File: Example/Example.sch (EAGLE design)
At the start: 9 parts, among them IC1 LM555D, J1 UX60-MB-5S8, SW1 MFS101D-6-Z

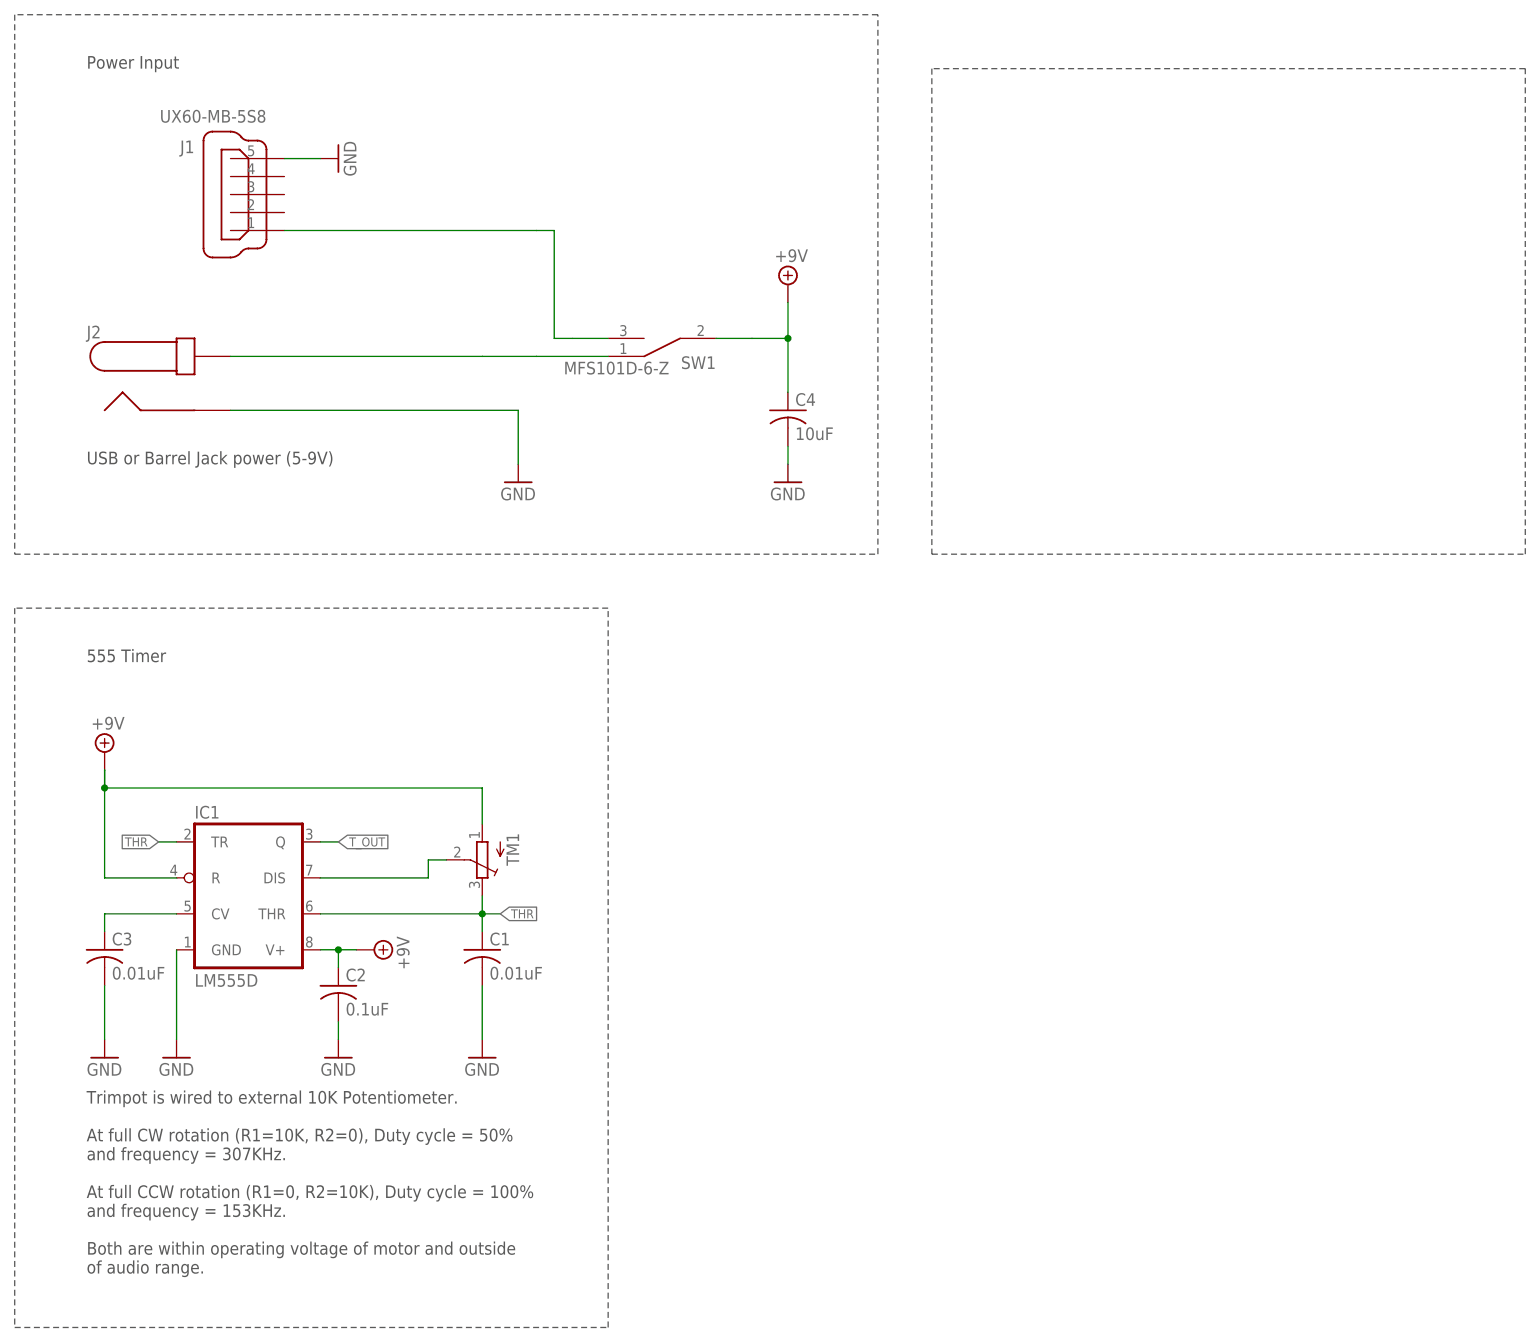
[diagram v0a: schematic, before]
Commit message: add
add parts
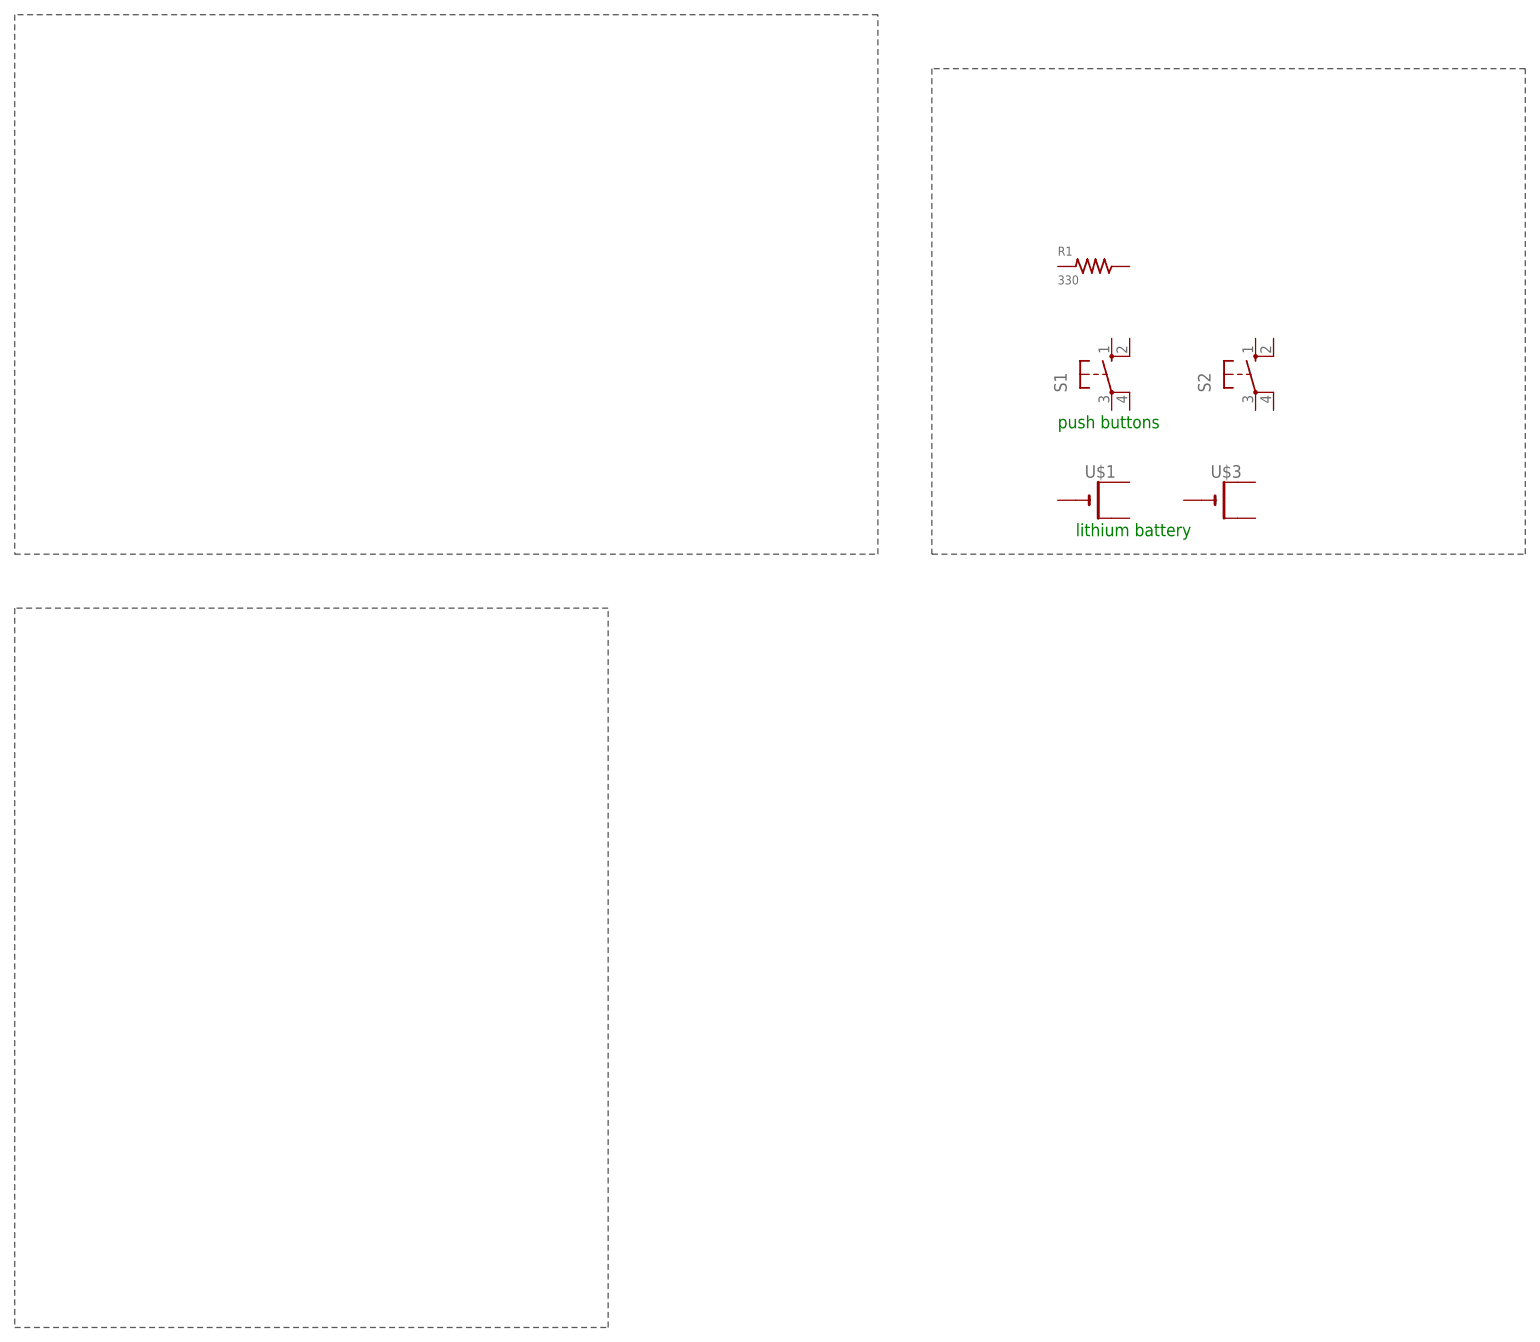
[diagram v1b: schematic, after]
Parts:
- removed C1, C3: 0.01uF, rcl:C-USC0603
- removed C2: 0.1uF, rcl:C-USC0603
- removed C4: 10uF, rcl:C-USC0603
- removed IC1: LM555D, adafruit:LM555D
- removed J1: UX60-MB-5S8, RoboJackets-Connectors:UX60-MB-5S8
- removed J2: (no value), RoboJackets-Connectors:PJ-037A
- removed SW1: MFS101D-6-Z, Example:MFS101D-6-Z
- removed TM1: (no value), adafruit:TRIMPOT3386
- added R1: 330, RoboJackets-Resistors:GHOST_RESISTOR
- added S1, S2: (no value), adafruit:40-XX
- added U$1, U$3: (no value), adafruit:CR1220SMT
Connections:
- removed net +9V: C2.1, C4.1, IC1.R, IC1.V+, SW1.COMMON, TM1.A
- removed net GND: C1.2, C2.2, C3.2, C4.2, IC1.GND, J1.5, J2.2
- removed net N$1: IC1.DIS, TM1.S
- removed net N$3: C3.1, IC1.CV
- removed net N$4: J1.1, SW1.B
- removed net N$6: J2.1, SW1.A
- removed net THR: C1.1, IC1.THR, IC1.TR, TM1.E
- removed net T_OUT: IC1.Q
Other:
- note added: "lithium battery"
- note added: "push buttons"
- note removed: "555 Timer"
- note removed: "Power Input"
- note removed: "Trimpot is wired to external 10K Potentiometer. At full CW rotation (R1=10K, R2=0), Duty cycle = 50% and frequency = 307KHz. At full CCW rotation (R1=0, R2=10K), Duty cycle = 100% and frequency = 153KHz. Both are within operating voltage of motor and outside of audio range."
- note removed: "USB or Barrel Jack power (5-9V)"

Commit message: Revert "add"
This reverts commit c6e4ebc28e4f55c76fdda87922b953a09ff3b68b.
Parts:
- removed R1: 330, RoboJackets-Resistors:GHOST_RESISTOR
- removed S1, S2: (no value), adafruit:40-XX
- removed U$1, U$3: (no value), adafruit:CR1220SMT
- added C1, C3: 0.01uF, rcl:C-USC0603
- added C2: 0.1uF, rcl:C-USC0603
- added C4: 10uF, rcl:C-USC0603
- added IC1: LM555D, adafruit:LM555D
- added J1: UX60-MB-5S8, RoboJackets-Connectors:UX60-MB-5S8
- added J2: (no value), RoboJackets-Connectors:PJ-037A
- added SW1: MFS101D-6-Z, Example:MFS101D-6-Z
- added TM1: (no value), adafruit:TRIMPOT3386
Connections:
- new net +9V: C2.1, C4.1, IC1.R, IC1.V+, SW1.COMMON, TM1.A
- new net GND: C1.2, C2.2, C3.2, C4.2, IC1.GND, J1.5, J2.2
- new net N$1: IC1.DIS, TM1.S
- new net N$3: C3.1, IC1.CV
- new net N$4: J1.1, SW1.B
- new net N$6: J2.1, SW1.A
- new net THR: C1.1, IC1.THR, IC1.TR, TM1.E
- new net T_OUT: IC1.Q
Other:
- note added: "555 Timer"
- note added: "Power Input"
- note added: "Trimpot is wired to external 10K Potentiometer. At full CW rotation (R1=10K, R2=0), Duty cycle = 50% and frequency = 307KHz. At full CCW rotation (R1=0, R2=10K), Duty cycle = 100% and frequency = 153KHz. Both are within operating voltage of motor and outside of audio range."
- note added: "USB or Barrel Jack power (5-9V)"
- note removed: "lithium battery"
- note removed: "push buttons"
